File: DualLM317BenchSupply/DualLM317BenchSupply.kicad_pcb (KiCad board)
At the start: 2 copper layers, 99.1 x 99.7 mm, 47 parts, among them CON101 BARREL_JACK, CON102 BARREL_JACK, P101 Vout+, P102 Vout-, SW101 SPDT, SW102 SPDT, SW103 SPDT, SW201 DP6T, U101 78L05, U102 LM317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

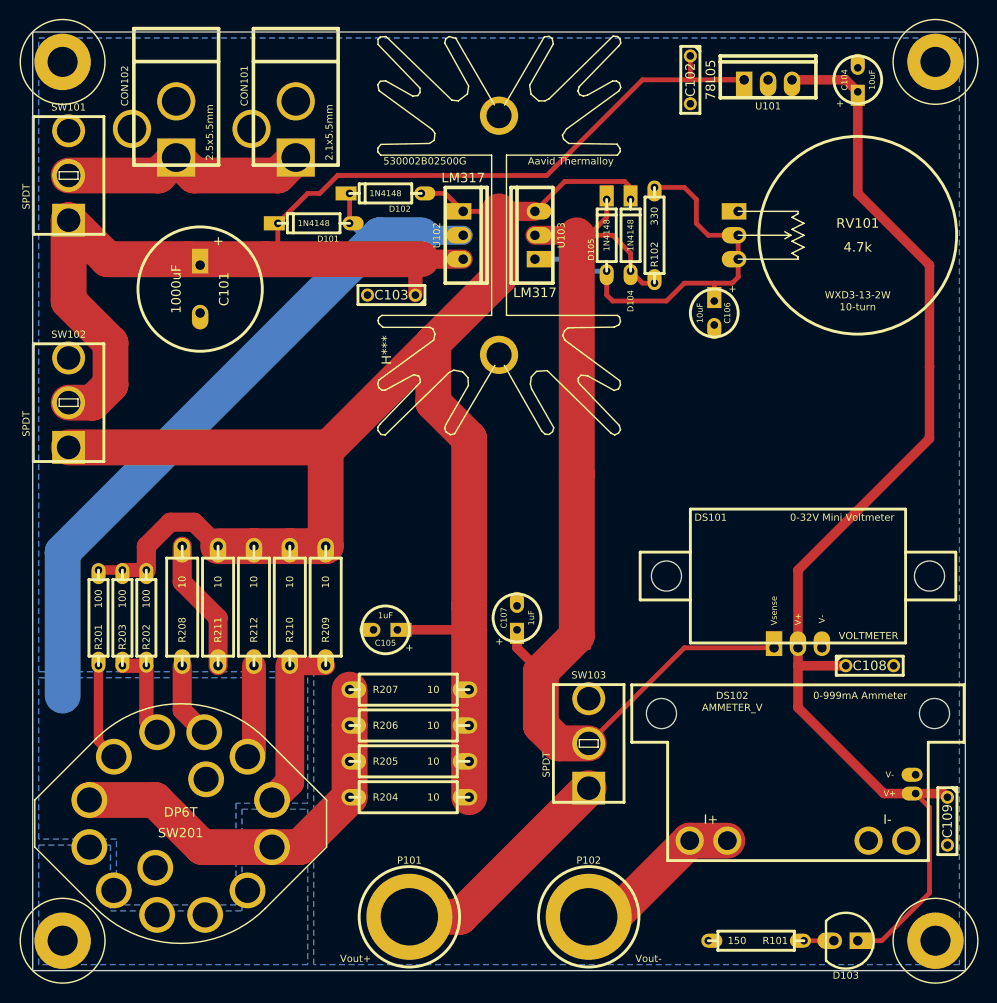
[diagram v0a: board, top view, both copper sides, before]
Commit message: tweaked board labels and created v1 gerbers
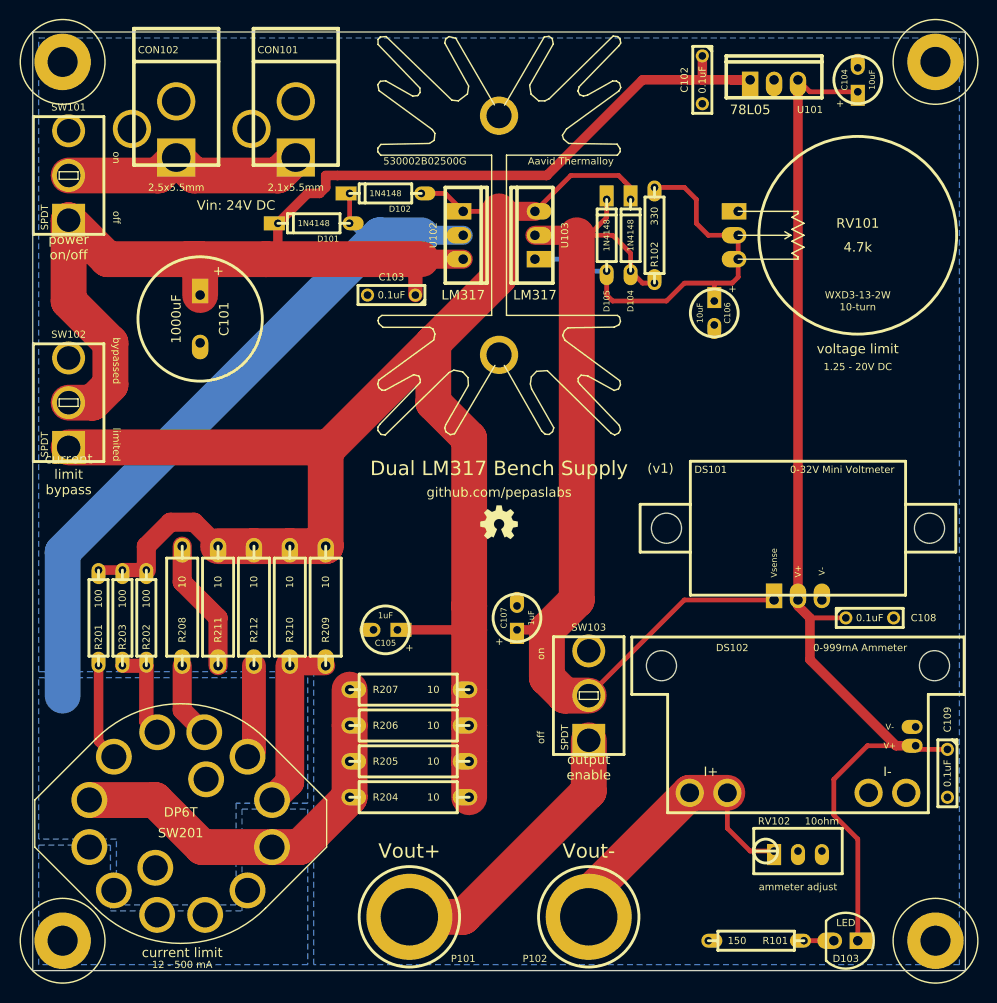
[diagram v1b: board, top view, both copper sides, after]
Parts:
- added G***: OSHW-logo_silkscreen-front_4mm, OSHW-logo_silkscreen-front_4mm, F.Cu at (186.1, 167.0)
- added RV102: 10ohm, 3296W, F.Cu at (217.8, 201.9)
- moved C108 5.08 mm to (225.4, 177.2)
- moved DS101 5.08 mm to (217.8, 167.6)
- moved SW103 5.08 mm to (195.6, 185.4)
- moved C109 5.08 mm to (233.7, 193.7)
- moved DS102 5.08 mm to (217.8, 182.2)
- moved C101 3.18 mm to (154.3, 142.9)
- moved C102 1.27 mm to (207.6, 120.0)
- moved U101 0.63 mm to (212.7, 120.0)
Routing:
- net N-000008: track 18.1 -> 31.3 mm
- net N-0000014: track 112.5 -> 102.4 mm
- net 5V: track 127.6 -> 119.7 mm
- net N-0000018: track 138.5 -> 146.2 mm
- net N-000005: track 24.7 -> 30.0 mm
- net /current_limit_r/R_LIM-: track 183.1 -> 183.6 mm
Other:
- board text added: "(v1)"
- board text added: "1.25 - 20V DC"
- board text added: "12 - 500 mA"
- board text added: "Dual LM317 Bench Supply"
- board text added: "Vin: 24V DC"
- board text added: "ammeter adjust"
- board text added: "bypassed"
- board text added: "current limit"
- board text added: "current limit bypass"
- board text added: "github.com/pepaslabs"
- board text added: "limited"
- board text added: "off"
- board text added: "on"
- board text added: "output enable"
- board text added: "power on/off"
- board text added: "voltage limit"

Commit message: adding back silkscreen
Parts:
- added G***: OSHW-logo_silkscreen-back_4mm, OSHW-logo_silkscreen-back_4mm, F.Cu at (186.1, 167.0)
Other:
- board text added: "(only use one power jack at a time)"
- board text added: "limits: 1: 13mA 2: 25mA 3: 63mA 4: 125mA 5: 250mA 6: 500mA"
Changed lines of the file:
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@@
     (area 134.870999 113.280999 237.239001 216.284001)
     (thickness 1.6)
-    (drawings 22)
+    (drawings 27)
     (tracks 159)
     (zones 0)
-    (modules 49)
+    (modules 50)
     (nets 19)
   )
@@
   )
   (setup
-    (last_trace_width 3.81)
+    (last_trace_width 0.254)
     (user_trace_width 0.508)
     (user_trace_width 1.016)
@@
       (xy -1.21158 1.79578)) (layer F.SilkS) (width 0.00254))
   )
+  (module OSHW-logo_silkscreen-back_4mm (layer F.Cu)
+    (at 186.055 167.005)
+    (fp_text reference G*** (at 0 2.1209) (layer B.SilkS) hide
+      (effects (font (size 0.18034 0.18034) (thickness 0.03556)))
+    )
+    (fp_text value OSHW-logo_silkscreen-back_4mm (at 0 -2.1209) (layer B.SilkS) hide
+      (effects (font (size 0.18034 0.18034) (thickness 0.03556)))
+    )
+    (fp_poly (pts (xy 1.21158 1.79578) (xy 1.19126 1.78562) (xy 1.143 1.75514) (xy 1.07696 1.71196)
+      (xy 0.99822 1.65862) (xy 0.91948 1.60528) (xy 0.85344 1.5621) (xy 0.80772 1.53162)
+      (xy 0.78994 1.52146) (xy 0.77978 1.524) (xy 0.74168 1.54432) (xy 0.6858 1.57226)
+      (xy 0.65532 1.5875) (xy 0.60452 1.61036) (xy 0.57912 1.61544) (xy 0.57658 1.60782)
+      (xy 0.55626 1.56972) (xy 0.52832 1.50368) (xy 0.49022 1.41732) (xy 0.44704 1.31572)
+      (xy 0.40132 1.2065) (xy 0.3556 1.09474) (xy 0.30988 0.98806) (xy 0.27178 0.89154)
+      (xy 0.23876 0.81534) (xy 0.21844 0.75946) (xy 0.21082 0.7366) (xy 0.21336 0.73152)
+      (xy 0.23876 0.70866) (xy 0.28194 0.67564) (xy 0.37846 0.5969) (xy 0.4699 0.48006)
+      (xy 0.52832 0.34798) (xy 0.5461 0.20066) (xy 0.53086 0.06604) (xy 0.47752 -0.0635)
+      (xy 0.38608 -0.18288) (xy 0.27432 -0.26924) (xy 0.14478 -0.32512) (xy 0 -0.3429)
+      (xy -0.1397 -0.32766) (xy -0.27178 -0.27432) (xy -0.39116 -0.18542) (xy -0.43942 -0.127)
+      (xy -0.508 -0.00762) (xy -0.54864 0.11938) (xy -0.55118 0.14986) (xy -0.5461 0.2921)
+      (xy -0.50546 0.42672) (xy -0.4318 0.5461) (xy -0.32766 0.64516) (xy -0.31496 0.65532)
+      (xy -0.2667 0.69088) (xy -0.23622 0.71374) (xy -0.21082 0.73406) (xy -0.38862 1.16586)
+      (xy -0.41656 1.23444) (xy -0.46736 1.35128) (xy -0.51054 1.45288) (xy -0.54356 1.53416)
+      (xy -0.56896 1.5875) (xy -0.57912 1.61036) (xy -0.57912 1.61036) (xy -0.59436 1.6129)
+      (xy -0.62738 1.6002) (xy -0.68834 1.57226) (xy -0.72898 1.55194) (xy -0.7747 1.52908)
+      (xy -0.79502 1.52146) (xy -0.8128 1.53162) (xy -0.85598 1.55956) (xy -0.91948 1.60274)
+      (xy -0.99568 1.65354) (xy -1.06934 1.70434) (xy -1.13792 1.75006) (xy -1.18618 1.78054)
+      (xy -1.21158 1.79324) (xy -1.21412 1.79324) (xy -1.23444 1.78054) (xy -1.27508 1.75006)
+      (xy -1.3335 1.69418) (xy -1.41478 1.6129) (xy -1.42748 1.6002) (xy -1.49606 1.52908)
+      (xy -1.55194 1.47066) (xy -1.59004 1.43002) (xy -1.60274 1.41224) (xy -1.60274 1.41224)
+      (xy -1.59004 1.38684) (xy -1.55956 1.33858) (xy -1.51384 1.27) (xy -1.4605 1.19126)
+      (xy -1.31826 0.98298) (xy -1.397 0.7874) (xy -1.41986 0.72898) (xy -1.45034 0.65532)
+      (xy -1.4732 0.60452) (xy -1.4859 0.58166) (xy -1.50622 0.57404) (xy -1.55956 0.56134)
+      (xy -1.6383 0.54356) (xy -1.72974 0.52832) (xy -1.81864 0.51054) (xy -1.89738 0.4953)
+      (xy -1.9558 0.48514) (xy -1.9812 0.48006) (xy -1.98628 0.47498) (xy -1.99136 0.46228)
+      (xy -1.99644 0.43688) (xy -1.99644 0.38862) (xy -1.99898 0.31242) (xy -1.99898 0.20066)
+      (xy -1.99898 0.1905) (xy -1.99644 0.08382) (xy -1.99644 0) (xy -1.9939 -0.05334)
+      (xy -1.98882 -0.07366) (xy -1.98882 -0.07366) (xy -1.96342 -0.08128) (xy -1.90754 -0.09144)
+      (xy -1.8288 -0.10922) (xy -1.73228 -0.127) (xy -1.7272 -0.127) (xy -1.63322 -0.14478)
+      (xy -1.55448 -0.16256) (xy -1.4986 -0.17526) (xy -1.47574 -0.18288) (xy -1.47066 -0.18796)
+      (xy -1.45034 -0.22606) (xy -1.4224 -0.28448) (xy -1.39192 -0.3556) (xy -1.36144 -0.42926)
+      (xy -1.3335 -0.49784) (xy -1.31572 -0.5461) (xy -1.31064 -0.56896) (xy -1.31064 -0.56896)
+      (xy -1.32588 -0.59182) (xy -1.3589 -0.64262) (xy -1.40462 -0.70866) (xy -1.4605 -0.78994)
+      (xy -1.46304 -0.79756) (xy -1.51892 -0.8763) (xy -1.5621 -0.94488) (xy -1.59258 -0.99314)
+      (xy -1.60274 -1.01346) (xy -1.60274 -1.016) (xy -1.58496 -1.03886) (xy -1.54432 -1.08458)
+      (xy -1.4859 -1.14554) (xy -1.41478 -1.21666) (xy -1.39192 -1.23698) (xy -1.31572 -1.31318)
+      (xy -1.26238 -1.36398) (xy -1.22682 -1.38938) (xy -1.21158 -1.397) (xy -1.21158 -1.39446)
+      (xy -1.18618 -1.38176) (xy -1.13538 -1.34874) (xy -1.0668 -1.30048) (xy -0.98552 -1.24714)
+      (xy -0.98044 -1.24206) (xy -0.9017 -1.18872) (xy -0.83566 -1.143) (xy -0.7874 -1.11252)
+      (xy -0.76708 -1.09982) (xy -0.762 -1.09982) (xy -0.73152 -1.10998) (xy -0.6731 -1.12776)
+      (xy -0.60452 -1.1557) (xy -0.53086 -1.18618) (xy -0.46228 -1.21412) (xy -0.41148 -1.23698)
+      (xy -0.38862 -1.24968) (xy -0.38862 -1.25222) (xy -0.37846 -1.28016) (xy -0.36576 -1.34112)
+      (xy -0.34798 -1.4224) (xy -0.3302 -1.52146) (xy -0.32766 -1.5367) (xy -0.30988 -1.63068)
+      (xy -0.29464 -1.70942) (xy -0.28194 -1.7653) (xy -0.27686 -1.78816) (xy -0.26416 -1.7907)
+      (xy -0.2159 -1.79324) (xy -0.14478 -1.79578) (xy -0.05842 -1.79578) (xy 0.03048 -1.79578)
+      (xy 0.11684 -1.79324) (xy 0.19304 -1.7907) (xy 0.24638 -1.78816) (xy 0.26924 -1.78308)
+      (xy 0.27178 -1.78054) (xy 0.2794 -1.7526) (xy 0.2921 -1.69164) (xy 0.30988 -1.61036)
+      (xy 0.32766 -1.5113) (xy 0.3302 -1.49352) (xy 0.34798 -1.39954) (xy 0.36576 -1.3208)
+      (xy 0.37592 -1.26746) (xy 0.38354 -1.24714) (xy 0.39116 -1.24206) (xy 0.42926 -1.22428)
+      (xy 0.49276 -1.19888) (xy 0.57404 -1.16586) (xy 0.75692 -1.0922) (xy 0.98044 -1.24714)
+      (xy 1.00076 -1.25984) (xy 1.08204 -1.31572) (xy 1.14808 -1.3589) (xy 1.1938 -1.38938)
+      (xy 1.21412 -1.39954) (xy 1.21412 -1.39954) (xy 1.23698 -1.37922) (xy 1.2827 -1.33858)
+      (xy 1.34366 -1.27762) (xy 1.41224 -1.20904) (xy 1.46558 -1.1557) (xy 1.52654 -1.0922)
+      (xy 1.56718 -1.05156) (xy 1.5875 -1.02362) (xy 1.59512 -1.00584) (xy 1.59258 -0.99568)
+      (xy 1.57988 -0.97282) (xy 1.54686 -0.92456) (xy 1.50114 -0.85598) (xy 1.44526 -0.77724)
+      (xy 1.39954 -0.70866) (xy 1.35128 -0.635) (xy 1.3208 -0.58166) (xy 1.3081 -0.55372)
+      (xy 1.31064 -0.54356) (xy 1.32842 -0.50038) (xy 1.35382 -0.4318) (xy 1.38684 -0.35306)
+      (xy 1.46558 -0.17526) (xy 1.58242 -0.15494) (xy 1.65354 -0.1397) (xy 1.7526 -0.12192)
+      (xy 1.84658 -0.10414) (xy 1.9939 -0.07366) (xy 1.99898 0.46482) (xy 1.97612 0.47498)
+      (xy 1.95326 0.4826) (xy 1.89992 0.49276) (xy 1.82118 0.508) (xy 1.72974 0.52578)
+      (xy 1.651 0.54102) (xy 1.57226 0.55626) (xy 1.51638 0.56642) (xy 1.49098 0.5715)
+      (xy 1.48336 0.58166) (xy 1.46304 0.61976) (xy 1.4351 0.68072) (xy 1.40462 0.75438)
+      (xy 1.37414 0.82804) (xy 1.3462 0.89916) (xy 1.32588 0.9525) (xy 1.31826 0.98044)
+      (xy 1.32842 1.00076) (xy 1.3589 1.04648) (xy 1.40208 1.11252) (xy 1.45542 1.19126)
+      (xy 1.5113 1.27) (xy 1.55448 1.33858) (xy 1.5875 1.38684) (xy 1.6002 1.40716)
+      (xy 1.59258 1.4224) (xy 1.5621 1.4605) (xy 1.50368 1.52146) (xy 1.41478 1.61036)
+      (xy 1.39954 1.62306) (xy 1.33096 1.69164) (xy 1.27 1.74498) (xy 1.22936 1.78308)
+      (xy 1.21158 1.79578)) (layer B.SilkS) (width 0.00254))
+  )
+  (gr_text "(v1)" (at 168.91 161.29) (layer B.SilkS)
+    (effects (font (size 1.016 1.016) (thickness 0.2032)) (justify mirror))
+  )
+  (gr_text github.com/pepaslabs (at 186.055 163.83) (layer B.SilkS)
+    (effects (font (size 1.016 1.016) (thickness 0.2032)) (justify mirror))
+  )
+  (gr_text "Dual LM317 Bench Supply" (at 186.055 161.29) (layer B.SilkS)
+    (effects (font (size 1.524 1.524) (thickness 0.3048)) (justify mirror))
+  )
+  (gr_text "limits:\n1: 13mA\n2: 25mA\n3: 63mA\n4: 125mA\n5: 250mA\n6: 500mA" (at 164.465 206.375) (layer F.SilkS)
+    (effects (font (size 0.762 0.762) (thickness 0.1524)) (justify left))
+  )
+  (gr_text "(only use one power jack at a time)" (at 158.115 116.84) (layer B.SilkS)
+    (effects (font (size 0.762 0.762) (thickness 0.1524)) (justify mirror))
+  )
   (gr_text off (at 145.415 134.62 270) (layer F.SilkS)

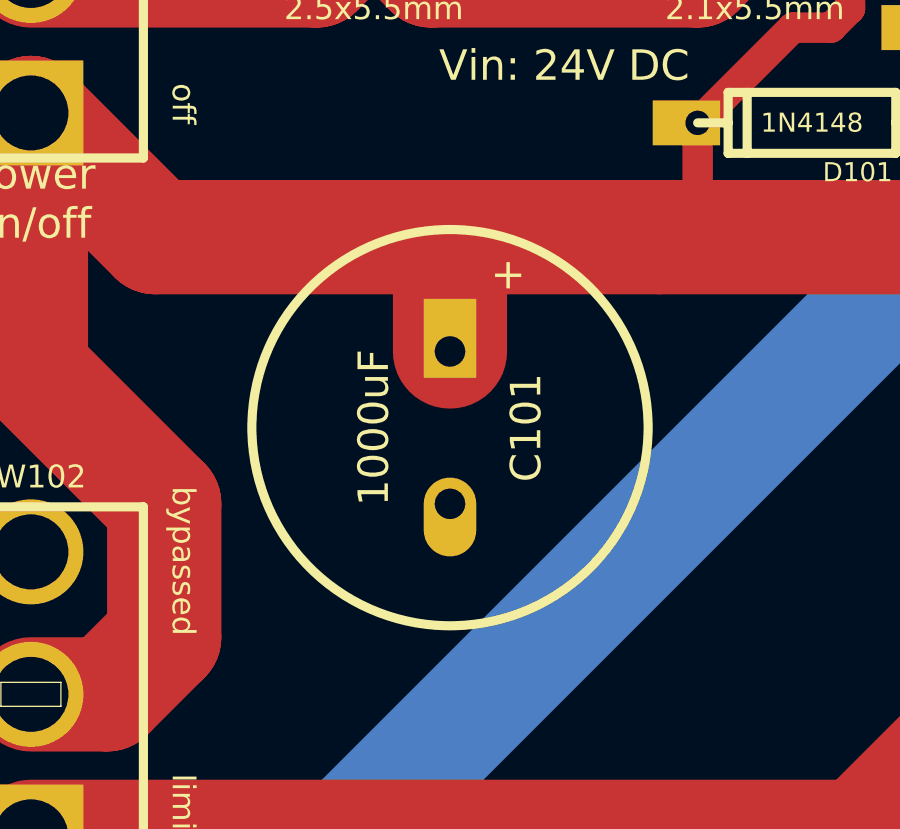
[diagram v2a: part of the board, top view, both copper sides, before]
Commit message: thinning cap trace for solderability
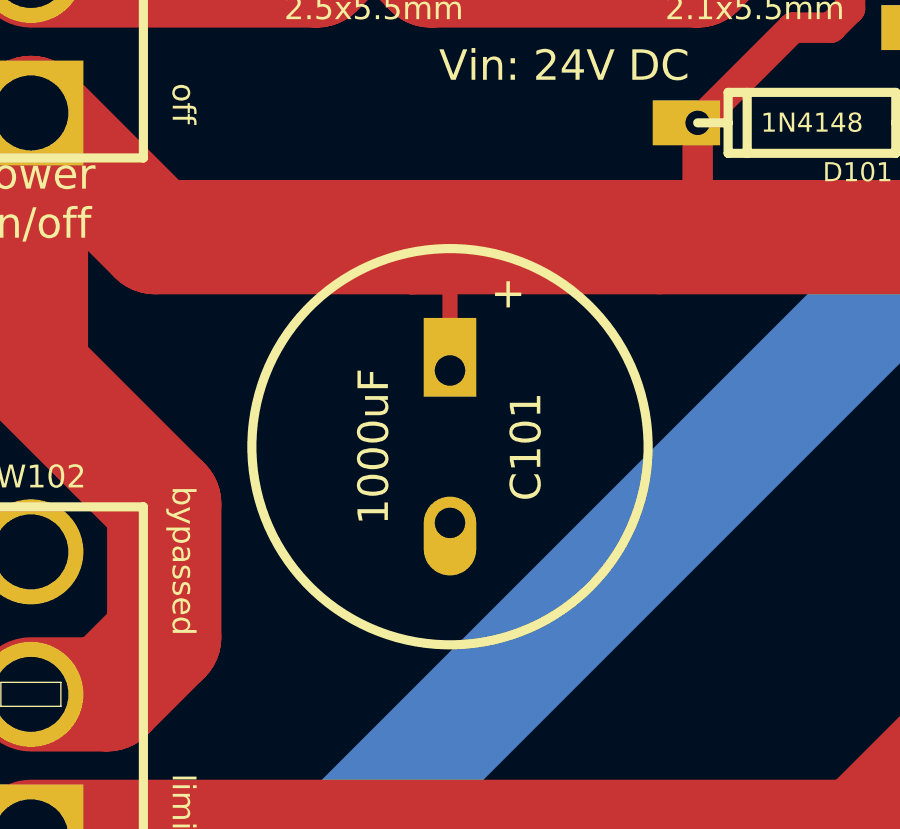
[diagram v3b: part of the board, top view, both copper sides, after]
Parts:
- moved C101 0.63 mm to (154.3, 143.5)
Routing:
- net N-0000018: track 146.2 -> 146.9 mm
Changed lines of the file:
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@@
   )
   (setup
-    (last_trace_width 0.254)
+    (last_trace_width 0.508)
     (user_trace_width 0.508)
     (user_trace_width 1.016)
@@
   )
   (module ELCAP_20_52_V (layer F.Cu)
-    (at 154.305 142.875 270)
+    (at 154.305 143.51 270)
     (descr "Electrolytic Capacitor, vertical, 0.2\" pins, 0.52\" body")
     (tags CP)
@@
   (segment (start 197.485 134.62) (end 195.58 136.525) (width 0.508) (layer F.Cu) (net 7))
   (segment (start 218.44 211.455) (end 221.615 211.455) (width 0.508) (layer F.Cu) (net 8))
-  (segment (start 154.305 142.875) (end 154.305 139.065) (width 3.81) (layer F.Cu) (net 9))
+  (segment (start 154.305 143.51) (end 154.305 139.065) (width 0.508) (layer F.Cu) (net 9) (status 400000))
   (segment (start 154.305 139.065) (end 153.035 139.065) (width 3.81) (layer F.Cu) (net 9))
   (segment (start 212.725 120.015) (end 210.82 120.015) (width 1.016) (layer F.Cu) (net 9))
